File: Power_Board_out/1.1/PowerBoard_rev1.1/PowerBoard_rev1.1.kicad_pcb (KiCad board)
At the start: 2 copper layers, 40 x 40 mm, 24 parts, among them J1 HMTSW-102-X-X-S-X, J2 HMTSW-102-X-X-S-X, J3 HMTSW-102-X-X-S-X, J4 HMTSW-102-X-X-S-X, J5 HMTSW-102-X-X-S-X, J6 HMTSW-102-X-X-S-X, J7 HMTSW-102-X-X-S-X, U1 DRV8410PWPR, U2 MCP73812T-420I-OT

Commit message: finished power board
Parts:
- added C7: 1uF, Capacitor_SMD:C_0201_0603Metric, F.Cu at (136.8, 42.8)
- added C8: 1uF, Capacitor_SMD:C_0201_0603Metric, F.Cu at (136.8, 44.6)
- added J8: 530470210, 53047-0210:CON_530470210_MOL, F.Cu at (157.1, 61.3)
- added R2: 2k, Resistor_SMD:R_01005_0402Metric, F.Cu at (136.7, 46.3)
- added R3: 2, Resistor_SMD:R_0805_2012Metric, F.Cu at (110.3, 45.5)
- added R4: 2, Resistor_SMD:R_0805_2012Metric, F.Cu at (110.3, 48.5)
- added U3: MCP73812T-420I-OT, Package_TO_SOT_SMD:SOT-23-5, F.Cu at (133.0, 44.2)
- J7: value HMTSW-102-X-X-S-X -> 530470210; footprint HMTSW-102-X-X-S-X:SAMTEC_HMTSW-102-X-X-S-X -> 53047-0210:CON_530470210_MOL
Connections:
- U1 pad 3: unconnected-(U1-AISEN-Pad3) -> Net-(U1-AISEN)
- U1 pad 6: unconnected-(U1-BISEN-Pad6) -> Net-(U1-BISEN)

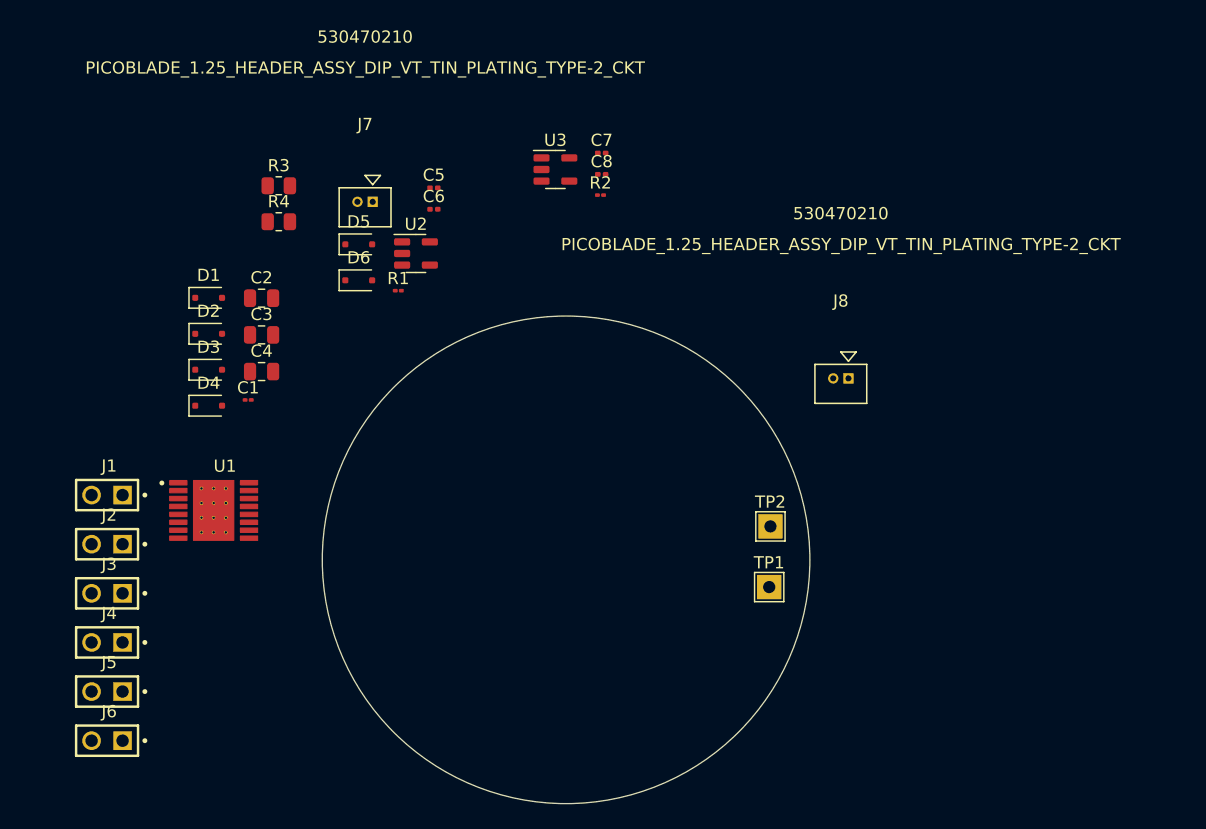
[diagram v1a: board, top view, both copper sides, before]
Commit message: fixing POE board symbols + circuit
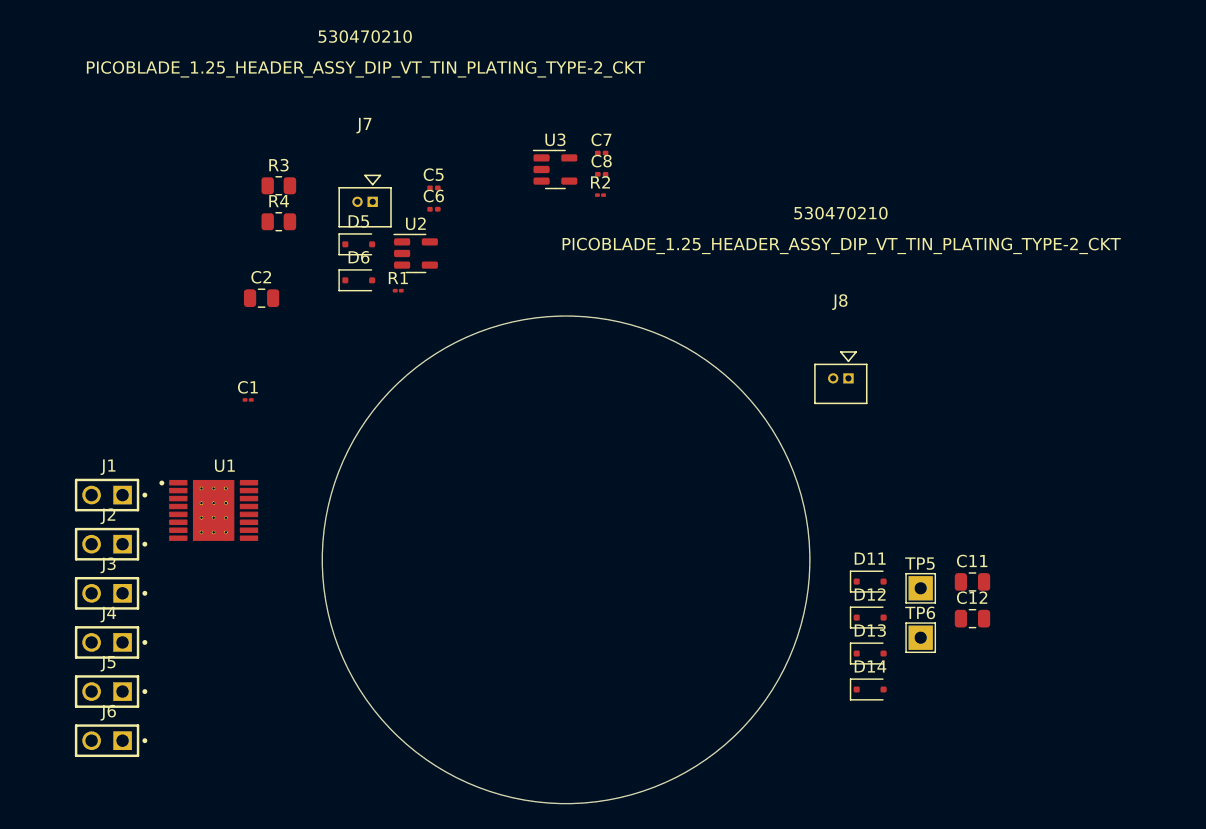
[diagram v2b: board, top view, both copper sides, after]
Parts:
- removed C3: 6nF, Capacitor_SMD:C_0805_2012Metric
- removed C4: 10uF, Capacitor_SMD:C_0805_2012Metric
- removed D1, D2, D3, D4: PMEG6010CEJ, Diode_SMD:D_SOD-323F
- removed TP1: COIL1, TestPoint:TestPoint_THTPad_2.0x2.0mm_Drill1.0mm
- removed TP2: COIL2, TestPoint:TestPoint_THTPad_2.0x2.0mm_Drill1.0mm
- added C11: 6nF, Capacitor_SMD:C_0805_2012Metric, F.Cu at (167.2, 78.0)
- added C12: 10uF, Capacitor_SMD:C_0805_2012Metric, F.Cu at (167.2, 81.0)
- added D11: PMEG6010CEJ, Diode_SMD:D_SOD-323F, F.Cu at (158.9, 78.0)
- added D12: PMEG6010CEJ, Diode_SMD:D_SOD-323F, F.Cu at (158.9, 80.9)
- added D13: PMEG6010CEJ, Diode_SMD:D_SOD-323F, F.Cu at (158.9, 83.9)
- added D14: PMEG6010CEJ, Diode_SMD:D_SOD-323F, F.Cu at (158.9, 86.8)
- added TP5: COIL1, TestPoint:TestPoint_THTPad_2.0x2.0mm_Drill1.0mm, F.Cu at (163.0, 78.5)
- added TP6: COIL2, TestPoint:TestPoint_THTPad_2.0x2.0mm_Drill1.0mm, F.Cu at (163.0, 82.6)
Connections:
- C5 pad 1: GND -> VCC
- C7 pad 1: GND -> VCC
- D6 pad 2: GND -> VCC
- U2 pad 1: GND -> VCC
- U2 pad 4: GND -> VCC
- U3 pad 1: GND -> VCC
- U3 pad 4: GND -> VCC

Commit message: power board layout
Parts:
- J7, J8, TP5, TP6: moved to B.Cu
- moved J3 56.1 mm to (149.8, 62.3)
- moved J6 54.2 mm to (143.0, 63.4)
- moved J7 51.9 mm to (142.9, 92.4)
- moved J2 49.3 mm to (143.0, 59.2)
- moved C2 46.6 mm to (148.6, 79.2), turned to -90 degrees
- moved J5 46.0 mm to (136.4, 64.6)
- moved C7 43.5 mm to (144.9, 85.5)
- moved C8 43.1 mm to (144.5, 87.0), turned to 90 degrees
- moved U3 43.0 mm to (142.0, 86.3), turned to 90 degrees
- moved C1 42.2 mm to (148.0, 76.0), turned to 90 degrees
- moved J1 41.6 mm to (136.4, 60.4)
- moved R4 40.0 mm to (137.2, 78.0), turned to -90 degrees
- moved R2 39.8 mm to (138.9, 86.1), turned to -90 degrees
- moved R3 39.0 mm to (137.2, 73.8), turned to 90 degrees
- moved U1 38.3 mm to (143.1, 75.9)
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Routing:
- net +BATT: track 0.00 -> 54.8 mm
- net GND: track 0.00 -> 27.2 mm, vias 0 -> 13
- net VCC: track 0.00 -> 17.0 mm, vias 0 -> 6
- net Net-(D11-K): track 0.00 -> 7.77 mm
- net Net-(D12-K): track 0.00 -> 7.63 mm
- net Net-(U1-BISEN): track 0.00 -> 3.10 mm
- net Net-(U1-AISEN): track 0.00 -> 3.10 mm
- net Net-(U3-PROG): track 0.00 -> 2.42 mm
- net Net-(U2-PROG): track 0.00 -> 1.90 mm
- added copper zone on In1.Cu, net GND
- added copper zone on In2.Cu, net VCC
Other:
- copper layers 2 -> 4

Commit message: group b2b
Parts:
- moved J6 9.85 mm to (133.3, 61.5), turned to 90 degrees
- moved J3 8.84 mm to (141.8, 66.1), turned to 180 degrees
- moved J1 5.41 mm to (141.8, 59.9), turned to 180 degrees
- moved J4 4.83 mm to (134.9, 66.0)
- moved J2 4.02 mm to (141.8, 63.0), turned to 180 degrees
- moved J5 3.13 mm to (136.4, 61.5), turned to -90 degrees
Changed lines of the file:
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@@
   )
   (footprint "HMTSW-102-X-X-S-X:SAMTEC_HMTSW-102-X-X-S-X" (layer "F.Cu")
-    (at 136.4488 60.3504)
+    (at 141.8425 59.94 180)
     (property "Availability" "In Stock")
     (property "Check_prices" "https://www.snapeda.com/parts/HMTSW-102-08-G-S-365/Samtec/view-part/?ref=eda")
@@
     (fp_circle (center 3.1 0) (end 3.2 0)
       (stroke (width 0.2) (type solid)) (fill none) (layer "F.Fab"))
-    (pad "01" thru_hole rect (at 1.27 0) (size 1.53 1.53) (drill 1.02) (layers "*.Cu" "*.Mask")
+    (pad "01" thru_hole rect (at 1.27 0 180) (size 1.53 1.53) (drill 1.02) (layers "*.Cu" "*.Mask")
       (net 12 "Net-(U1-BOUT1)") (pinfunction "01") (pintype "passive") (solder_mask_margin 0.102))
-    (pad "02" thru_hole circle (at -1.27 0) (size 1.53 1.53) (drill 1.02) (layers "*.Cu" "*.Mask")
+    (pad "02" thru_hole circle (at -1.27 0 180) (size 1.53 1.53) (drill 1.02) (layers "*.Cu" "*.Mask")
       (net 13 "Net-(U1-BOUT2)") (pinfunction "02") (pintype "passive") (solder_mask_margin 0.102))
   )
@@
   )
   (footprint "HMTSW-102-X-X-S-X:SAMTEC_HMTSW-102-X-X-S-X" (layer "F.Cu")
-    (at 142.9512 63.4492)
+    (at 133.3 61.4725 90)
     (property "Availability" "In Stock")
     (property "Check_prices" "https://www.snapeda.com/parts/HMTSW-102-08-G-S-365/Samtec/view-part/?ref=eda")
@@
     (property "SnapEDA_Link" "https://www.snapeda.com/parts/HMTSW-102-08-G-S-365/Samtec/view-part/?ref=snap")
     (attr through_hole)
-    (fp_text reference "J6" (at 0.175 -2.385) (layer "F.SilkS")
+    (fp_text reference "J6" (at 0.175 -2.385 90) (layer "F.SilkS")
         (effects (font (size 1 1) (thickness 0.15)))
     )
-    (fp_text value "HMTSW-102-X-X-S-X" (at 12.24 2.365) (layer "F.Fab")
+    (fp_text value "HMTSW-102-X-X-S-X" (at 12.24 2.365 90) (layer "F.Fab")
         (effects (font (size 1 1) (thickness 0.15)))
     )
@@
     (fp_circle (center 3.1 0) (end 3.2 0)
       (stroke (width 0.2) (type solid)) (fill none) (layer "F.Fab"))
-    (pad "01" thru_hole rect (at 1.27 0) (size 1.53 1.53) (drill 1.02) (layers "*.Cu" "*.Mask")
+    (pad "01" thru_hole rect (at 1.27 0 90) (size 1.53 1.53) (drill 1.02) (layers "*.Cu" "*.Mask")
       (net 16 "DRV_FAULT") (pinfunction "01") (pintype "passive") (solder_mask_margin 0.102))
-    (pad "02" thru_hole circle (at -1.27 0) (size 1.53 1.53) (drill 1.02) (layers "*.Cu" "*.Mask")
+    (pad "02" thru_hole circle (at -1.27 0 90) (size 1.53 1.53) (drill 1.02) (layers "*.Cu" "*.Mask")
       (net 17 "DRV_SLEEP") (pinfunction "02") (pintype "passive") (solder_mask_margin 0.102))
   )
@@
   )
   (footprint "HMTSW-102-X-X-S-X:SAMTEC_HMTSW-102-X-X-S-X" (layer "F.Cu")
-    (at 130.048 65.8876)
+    (at 134.88 65.99)
     (property "Availability" "In Stock")
     (property "Check_prices" "https://www.snapeda.com/parts/HMTSW-102-08-G-S-365/Samtec/view-part/?ref=eda")
@@
   )
   (footprint "HMTSW-102-X-X-S-X:SAMTEC_HMTSW-102-X-X-S-X" (layer "F.Cu")
-    (at 143.002 59.182)
+    (at 141.79 63.01 180)
     (property "Availability" "In Stock")
     (property "Check_prices" "https://www.snapeda.com/parts/HMTSW-102-08-G-S-365/Samtec/view-part/?ref=eda")
@@
     (fp_circle (center 3.1 0) (end 3.2 0)
       (stroke (width 0.2) (type solid)) (fill none) (layer "F.Fab"))
-    (pad "01" thru_hole rect (at 1.27 0) (size 1.53 1.53) (drill 1.02) (layers "*.Cu" "*.Mask")
+    (pad "01" thru_hole rect (at 1.27 0 180) (size 1.53 1.53) (drill 1.02) (layers "*.Cu" "*.Mask")
       (net 14 "Net-(U1-AOUT1)") (pinfunction "01") (pintype "passive") (solder_mask_margin 0.102))
-    (pad "02" thru_hole circle (at -1.27 0) (size 1.53 1.53) (drill 1.02) (layers "*.Cu" "*.Mask")
+    (pad "02" thru_hole circle (at -1.27 0 180) (size 1.53 1.53) (drill 1.02) (layers "*.Cu" "*.Mask")
       (net 15 "Net-(U1-AOUT2)") (pinfunction "02") (pintype "passive") (solder_mask_margin 0.102))
   )
@@
   )
   (footprint "HMTSW-102-X-X-S-X:SAMTEC_HMTSW-102-X-X-S-X" (layer "F.Cu")
-    (at 149.7699 62.2808)
+    (at 141.79 66.08 180)
     (property "Availability" "In Stock")
     (property "Check_prices" "https://www.snapeda.com/parts/HMTSW-102-08-G-S-365/Samtec/view-part/?ref=eda")
@@
     (fp_circle (center 3.1 0) (end 3.2 0)
       (stroke (width 0.2) (type solid)) (fill none) (layer "F.Fab"))
-    (pad "01" thru_hole rect (at 1.27 0) (size 1.53 1.53) (drill 1.02) (layers "*.Cu" "*.Mask")
+    (pad "01" thru_hole rect (at 1.27 0 180) (size 1.53 1.53) (drill 1.02) (layers "*.Cu" "*.Mask")
       (net 1 "GND") (pinfunction "01") (pintype "passive") (solder_mask_margin 0.102))
-    (pad "02" thru_hole circle (at -1.27 0) (size 1.53 1.53) (drill 1.02) (layers "*.Cu" "*.Mask")
+    (pad "02" thru_hole circle (at -1.27 0 180) (size 1.53 1.53) (drill 1.02) (layers "*.Cu" "*.Mask")
       (net 18 "VDC") (pinfunction "02") (pintype "passive") (solder_mask_margin 0.102))
   )
   (footprint "HMTSW-102-X-X-S-X:SAMTEC_HMTSW-102-X-X-S-X" (layer "F.Cu")
-    (at 136.398 64.6176)
+    (at 136.41 61.4875 -90)
     (property "Availability" "In Stock")
     (property "Check_prices" "https://www.snapeda.com/parts/HMTSW-102-08-G-S-365/Samtec/view-part/?ref=eda")
@@
     (property "SnapEDA_Link" "https://www.snapeda.com/parts/HMTSW-102-08-G-S-365/Samtec/view-part/?ref=snap")
     (attr through_hole)
-    (fp_text reference "J5" (at 0.175 -2.385) (layer "F.SilkS")
+    (fp_text reference "J5" (at 0.175 -2.385 90) (layer "F.SilkS")
         (effects (font (size 1 1) (thickness 0.15)))
     )
-    (fp_text value "HMTSW-102-X-X-S-X" (at 12.24 2.365) (layer "F.Fab")
+    (fp_text value "HMTSW-102-X-X-S-X" (at 12.24 2.365 90) (layer "F.Fab")
         (effects (font (size 1 1) (thickness 0.15)))
     )
@@
     (fp_circle (center 3.1 0) (end 3.2 0)
       (stroke (width 0.2) (type solid)) (fill none) (layer "F.Fab"))
-    (pad "01" thru_hole rect (at 1.27 0) (size 1.53 1.53) (drill 1.02) (layers "*.Cu" "*.Mask")
+    (pad "01" thru_hole rect (at 1.27 0 270) (size 1.53 1.53) (drill 1.02) (layers "*.Cu" "*.Mask")
       (net 5 "MOTOR2_BIN2") (pinfunction "01") (pintype "passive") (solder_mask_margin 0.102))
-    (pad "02" thru_hole circle (at -1.27 0) (size 1.53 1.53) (drill 1.02) (layers "*.Cu" "*.Mask")
+    (pad "02" thru_hole circle (at -1.27 0 270) (size 1.53 1.53) (drill 1.02) (layers "*.Cu" "*.Mask")
       (net 6 "MOTOR2_BIN1") (pinfunction "02") (pintype "passive") (solder_mask_margin 0.102))
   )

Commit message: POE1 board
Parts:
- moved J1 0.72 mm to (142.2, 60.6)
- moved J2 0.70 mm to (142.2, 63.6)
- moved C2 0.61 mm to (149.3, 79.1)
- moved J4 0.61 mm to (135.3, 66.4)
- moved J3 0.60 mm to (142.2, 66.5)
- moved J5 0.60 mm to (136.9, 61.9)
- moved J6 0.60 mm to (133.7, 61.9)
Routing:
- net MOTOR2_BIN1: track 0.00 -> 31.3 mm, vias 0 -> 1
- net MOTOR2_BIN2: track 0.00 -> 29.9 mm, vias 0 -> 1
- net Net-(U1-BOUT2): track 0.00 -> 27.6 mm, vias 0 -> 1
- net DRV_FAULT: track 0.00 -> 25.7 mm
- net Net-(U1-BOUT1): track 0.00 -> 20.5 mm, vias 0 -> 2
- net MOTOR1_AIN2: track 0.00 -> 16.6 mm
- net DRV_SLEEP: track 0.00 -> 16.5 mm
- net MOTOR1_AIN1: track 0.00 -> 15.9 mm
- net Net-(U1-AOUT2): track 0.00 -> 15.5 mm, vias 0 -> 1
- net Net-(U1-AOUT1): track 0.00 -> 12.7 mm, vias 0 -> 1
- net +BATT: track 54.8 -> 66.0 mm
- net VDC: track 0.00 -> 8.25 mm
- net VCC: track 17.0 -> 18.6 mm, vias 6 -> 7

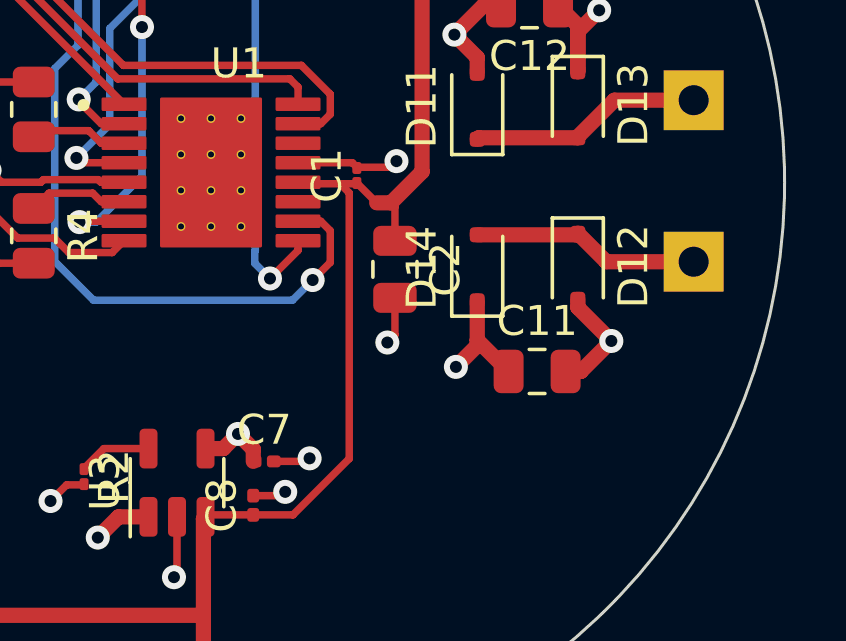
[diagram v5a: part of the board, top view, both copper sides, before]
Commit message: updated power
finished swapping power board bulk cap, new POE board schematic
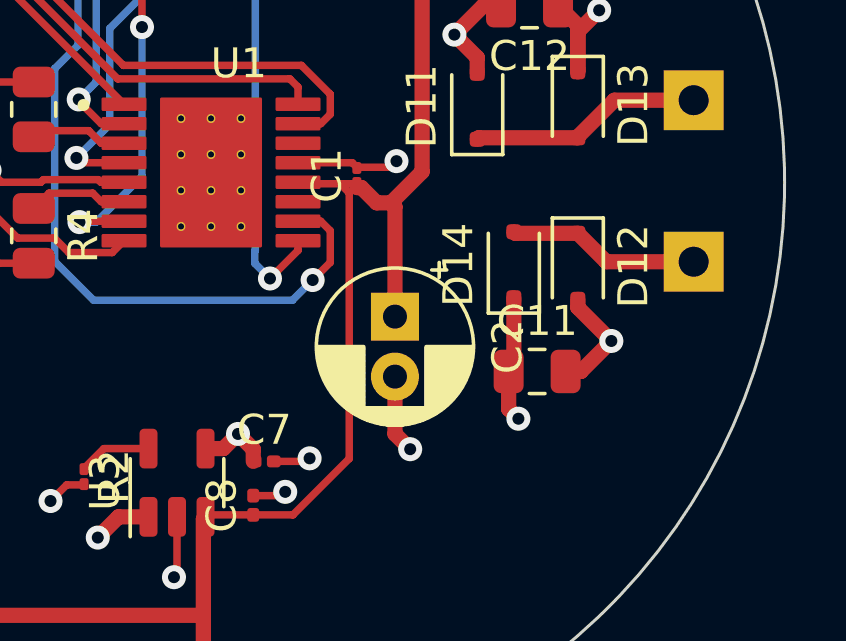
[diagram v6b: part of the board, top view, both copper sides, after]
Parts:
- C2: footprint Capacitor_SMD:C_0805_2012Metric -> Capacitor_THT:CP_Radial_D5.0mm_P2.00mm
- moved C2 1.57 mm to (149.3, 80.7)
- moved D14 1.22 mm to (153.2, 79.0)
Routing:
- net +BATT: track 66.0 -> 68.5 mm
- net Net-(D12-K): track 7.63 -> 6.41 mm
- net GND: track 27.2 -> 28.2 mm

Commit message: updates
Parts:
- C1: footprint Capacitor_SMD:C_01005_0402Metric -> Capacitor_SMD:C_0402_1005Metric
- R1: footprint Resistor_SMD:R_01005_0402Metric -> Resistor_SMD:R_0201_0603Metric
- moved C1 0.51 mm to (148.2, 76.5)
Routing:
- net +BATT: track 68.5 -> 64.9 mm
- net GND: track 28.2 -> 28.8 mm

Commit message: updated power
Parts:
- C1: footprint Capacitor_SMD:C_0402_1005Metric -> Capacitor_SMD:C_0603_1608Metric
- R2: footprint Resistor_SMD:R_01005_0402Metric -> Resistor_SMD:R_0201_0603Metric
- moved C1 0.19 mm to (148.2, 76.3)
